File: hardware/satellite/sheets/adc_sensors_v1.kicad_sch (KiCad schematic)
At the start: 7 parts, among them J2 Conn_01x03, J3 Conn_01x03, J4 Conn_01x03, J5 Conn_01x03, U2 ADS1115IDGS

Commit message: fix(satellite): Consolidate shared libraries, fix MDX/links, and update JST PA LCSC part (#24)
* Consolidate Hub and Satellite libraries into shared hardware/libraries

* Add SunSprout logo to Satellite silkscreen and refresh documentation assets

* Fix MDX compilation error and broken links in satellite documentation

* Update DS18B20 and moisture probe connectors to JST PA with LCSC part C131339
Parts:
- J2, J3, J4, J5: LCSC Part C157929 -> C131339
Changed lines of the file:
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@@
 			)
 		)
-		(property "LCSC Part" "C157929"
+		(property "LCSC Part" "C131339"
 			(at 38.1 38.1 0)
 			(hide yes)
@@
 			)
 		)
-		(property "LCSC Part" "C157929"
+		(property "LCSC Part" "C131339"
 			(at 38.1 63.5 0)
 			(hide yes)
@@
 			)
 		)
-		(property "LCSC Part" "C157929"
+		(property "LCSC Part" "C131339"
 			(at 38.1 88.9 0)
 			(hide yes)
@@
 			)
 		)
-		(property "LCSC Part" "C157929"
+		(property "LCSC Part" "C131339"
 			(at 38.1 114.3 0)
 			(hide yes)

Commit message: Improve Hub PCB layout, power loops, and sensing; add design review TODOs
- Hub PCB:
  - BQ25798 SW1/SW2 nodes: upgrade to 0.3mm neck with 3 parallel vias at IC and 2 at L1, plus B.Cu polygon pours
  - High-frequency loops: widen PMID and SYS connections with solid polygon pours to decoupling caps
  - Bootstrap caps: retain C317/C318 on F.Cu to preserve single-sided SMT assembly per TI 8.4.1 guidelines
  - Battery paths: cover U8 pins 22/23 with 0.8mm polygon pour and widen VBAT_RAW / VBAT_PROTECTED traces
  - Fuel gauge shunt: route FG_SRN and BATT_RTN as a 2.78mm matched parallel Kelvin pair from inner pad edges
  - ESP32-C5: rewire boot button SW2 to GPIO28; expose GPIO0 on header J7 pin 3
  - Flashing test points: add TP16-TP19 on B.Cu for single-sided bed-of-nails flashing
  - Layer balance: add full-board GND fill zone on In2.Cu and In3.Cu to balance copper density
- Add TODO tracking checklists for Satellite and Hub PCB reviews
- Add Hub pinout generator tool and update pinout documentation
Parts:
- JP1: now left out of the parts list
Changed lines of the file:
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@@
 		(body_style 1)
 		(exclude_from_sim no)
-		(in_bom yes)
+		(in_bom no)
 		(on_board yes)
-		(in_pos_files yes)
+		(in_pos_files no)
 		(dnp no)
 		(property "Reference" "JP1"

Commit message: feat(hardware): complete satellite pcb routing and layout review fixes
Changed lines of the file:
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@@
 		(dnp no)
 		(property "Reference" "U2"
-			(at 93.98 67.31 0)
+			(at 91.694 59.436 0)
 			(show_name no)
 			(do_not_autoplace no)
@@
 		)
 		(property "Value" "ADS1115IDGS"
-			(at 93.98 69.85 0)
+			(at 91.186 62.23 0)
 			(show_name no)
 			(do_not_autoplace no)
@@
 			)
 		)
-		(property "Datasheet" ""
+		(property "Datasheet" "http://www.ti.com/lit/ds/symlink/ads1113.pdf"
 			(at 101.6 76.2 0)
 			(hide yes)
@@
 			)
 		)
-		(property "Description" ""
+		(property "Description" "Ultra-Small, Low-Power, I2C-Compatible, 860-SPS, 16-Bit ADCs With Internal Reference, Oscillator, and Programmable Comparator, VSSOP-10"
 			(at 101.6 76.2 0)
+			(hide yes)
 			(show_name no)
 			(do_not_autoplace no)

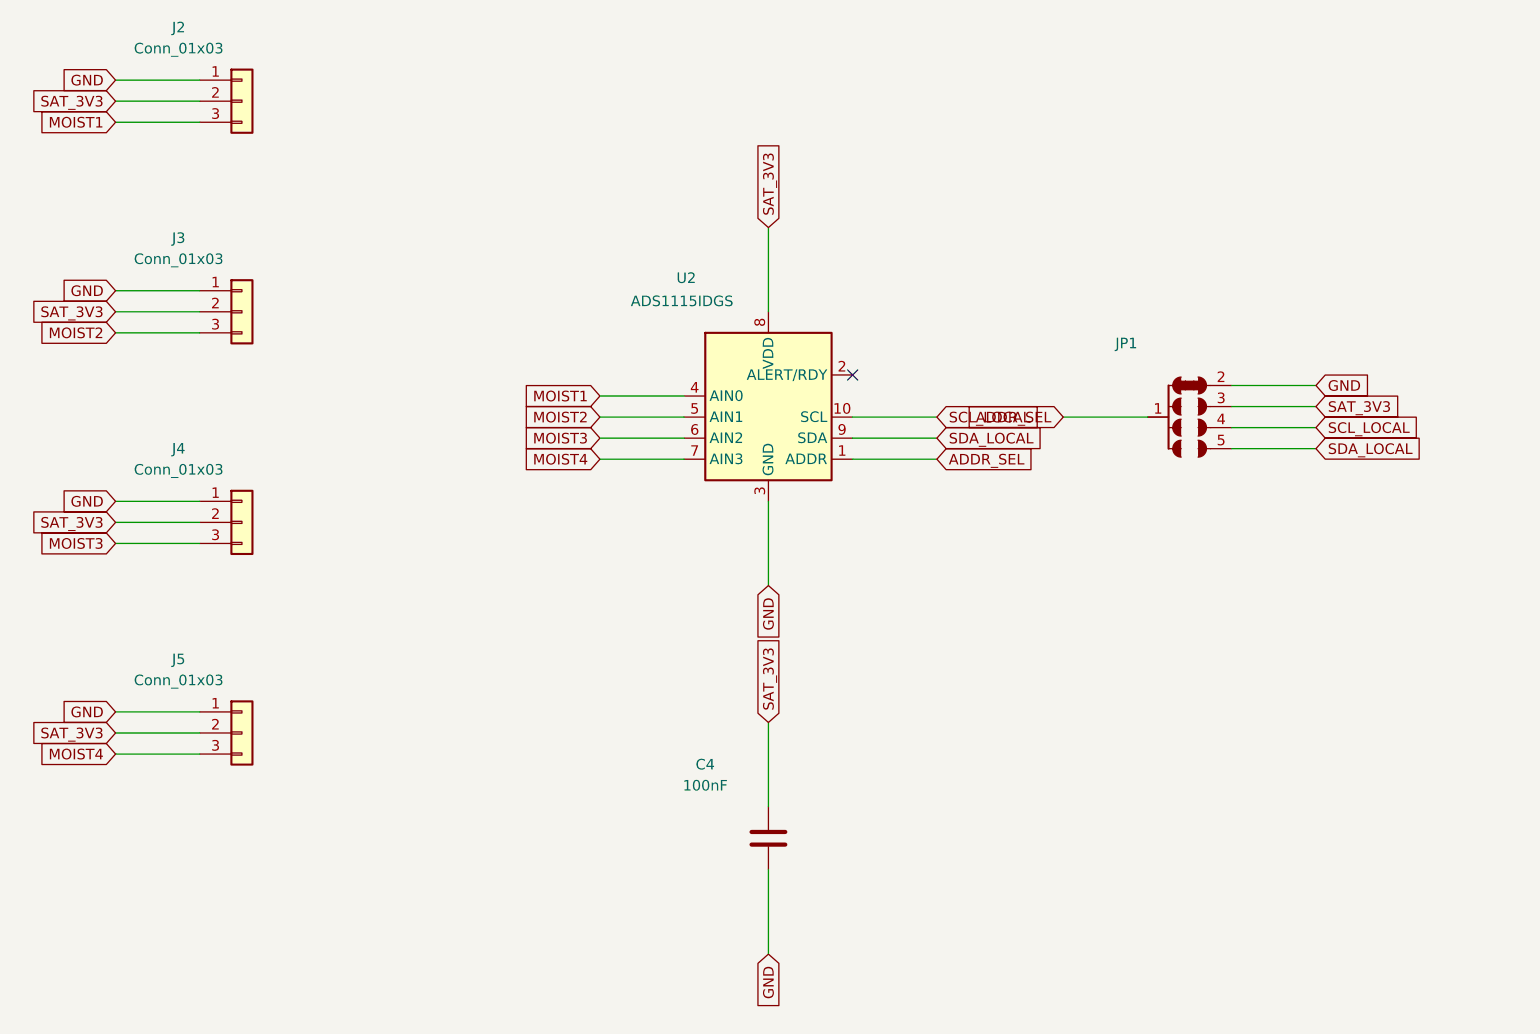
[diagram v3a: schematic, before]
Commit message: feat(satellite): redesign power entry architecture, solder jumpers, and address footprints
- Decouple raw cable power (Pair 1: RJ45_VCC_1/GND_1, Pair 3: RJ45_VCC_2/GND_2) onto 4P header J7
- Add 2P header J9 for local satellite power (SAT_3V3, GND) to support external regulation
- Add normally-closed cuttable jumpers JP18 (VCC_1 <-> SAT_3V3) and JP17 (GND_1 <-> GND)
- Tie PCA9615 VDDB, diff termination bias (R3/R5/R6/R8), and TVS U4 to RJ45_VCC_1/GND_1
- Place bulk cap C1 (22uF) across RJ45_VCC_1 and RJ45_GND_1 at cable entry
- Split inner planes: continuous RJ45_GND_1 reference on In2.Cu under B.Cu diff pairs; In1.Cu split (SAT GND, RJ45 GND, VCC2)
- Update 1-Wire address jumper footprint with +1/+2 bit-weighting notation and 0x18 default
- Remove deprecated pcb-pipeline generator scripts
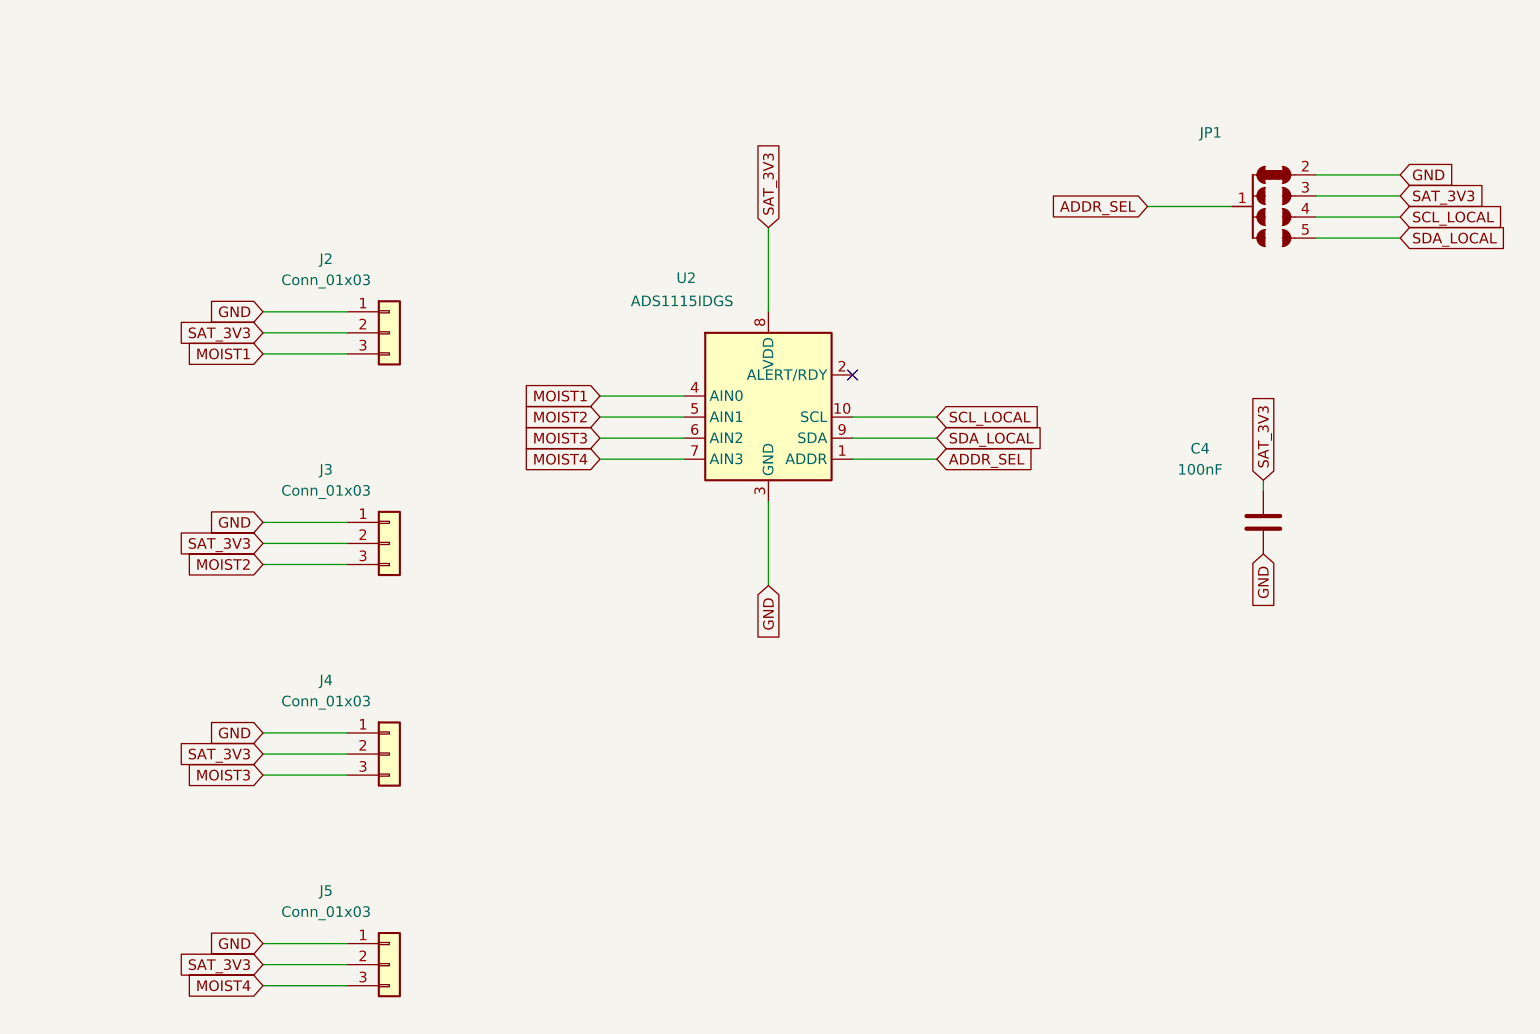
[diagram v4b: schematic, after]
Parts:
- C4: footprint Capacitor_SMD:C_0603_1608Metric -> Capacitor_SMD:C_0805_2012Metric_Pad1.18x1.45mm_HandSolder; LCSC Part C14663 -> C28233
- JP1: footprint project:SolderJumper-4_P1.3mm_Bridged12_RoundedPad1.0x1.5mm -> project:ADCAddrJumper1mmPads
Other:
- moved on the sheet: C4, J2, J3, J4, J5, JP1
